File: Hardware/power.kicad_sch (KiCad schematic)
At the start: 60 parts, among them J201 Line, J202 Earth, J203 Neutral, J204 44472-0453, SW201 SW_DPST, T201 B82732R2142, T202 14A-56-28, U201 LM7912, U202 LM2574N-3.3, U203 LM2596T-5, U204 LM2596T-12

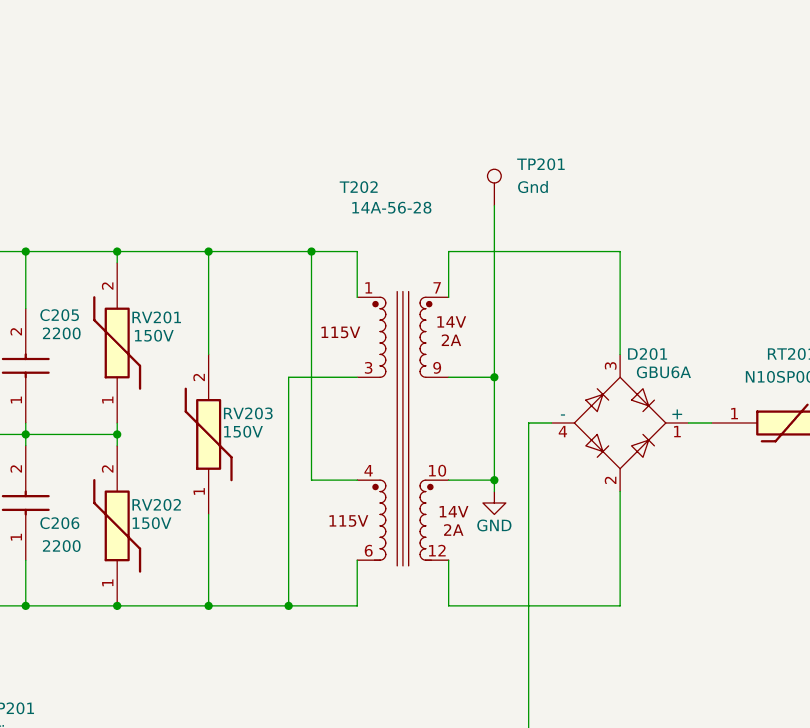
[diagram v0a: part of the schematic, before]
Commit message: updated schematics
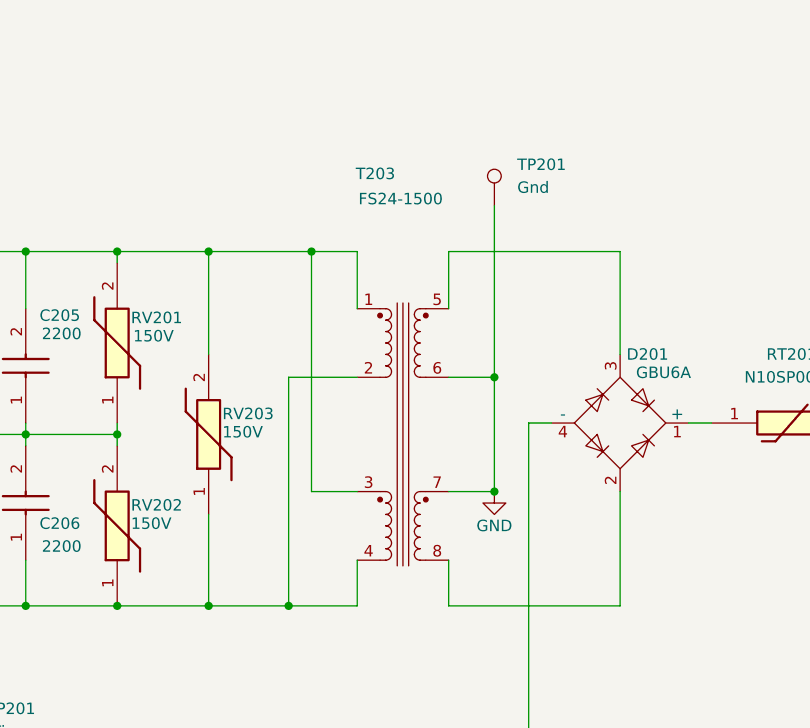
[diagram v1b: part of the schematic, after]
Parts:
- removed T202: 14A-56-28, Transformers_Signal:14A-56, symbol DH_Transformers_Power:14A-56-28
- added T203: FS24-1500, DH_Transformers_Triad:FS-36VA, symbol DH_Transformers_Triad:FS24-1500
- JP201: footprint (none) -> Jumper:SolderJumper-2_P1.3mm_Bridged_RoundedPad1.0x1.5mm
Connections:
- net GND: now also T203.6, T203.7
- net at C204.2, C205.2, RV201.2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: now also T203.1, T203.3
- net at D201.2: now also T203.8
- net at C204.1, C206.1, RV202.1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: now also T203.2, T203.4
- net at D201.3: now also T203.5
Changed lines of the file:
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@@
 	)
 	(junction
+		(at 200.66 140.97)
+		(diameter 0)
+		(color 0 0 0 0)
+	)
+	(junction
 		(at 148.59 134.62)
 		(diameter 0)
@@
 	)
 	(junction
-		(at 200.66 139.7)
-		(diameter 0)
-		(color 0 0 0 0)
-	)
-	(junction
 		(at 267.97 133.35)
 		(diameter 0)
@@
 	(wire
 		(pts
-			(xy 185.42 114.3) (xy 185.42 119.38)
+			(xy 185.42 114.3) (xy 185.42 120.65)
 		)
 		(stroke
@@
 	(wire
 		(pts
-			(xy 180.34 114.3) (xy 180.34 139.7)
+			(xy 180.34 114.3) (xy 180.34 140.97)
 		)
 		(stroke
@@
 	(wire
 		(pts
-			(xy 195.58 139.7) (xy 200.66 139.7)
+			(xy 195.58 140.97) (xy 200.66 140.97)
 		)
 		(stroke
@@
 	(wire
 		(pts
-			(xy 200.66 139.7) (xy 200.66 140.97)
-		)
-		(stroke
-			(width 0)
-			(type default)
-		)
-	)
-	(wire
-		(pts
 			(xy 307.34 90.17) (xy 339.09 90.17)
 		)
@@
 	(wire
 		(pts
-			(xy 195.58 114.3) (xy 195.58 119.38)
+			(xy 195.58 114.3) (xy 195.58 120.65)
 		)
 		(stroke
@@
 	(wire
 		(pts
-			(xy 200.66 139.7) (xy 200.66 128.27)
-		)
-		(stroke
-			(width 0)
-			(type default)
-		)
-	)
-	(wire
-		(pts
 			(xy 267.97 185.42) (xy 285.75 185.42)
 		)
@@
 	(wire
 		(pts
-			(xy 185.42 139.7) (xy 180.34 139.7)
+			(xy 185.42 140.97) (xy 180.34 140.97)
 		)
 		(stroke
@@
 	(wire
 		(pts
+			(xy 200.66 128.27) (xy 200.66 140.97)
+		)
+		(stroke
+			(width 0)
+			(type default)
+		)
+	)
+	(wire
+		(pts
 			(xy 364.49 60.96) (xy 372.11 60.96)
 		)
@@
 	)
 	(symbol
-		(lib_id "DH_Transformers_Power:14A-56-28")
-		(at 190.5 132.08 0)
-		(unit 1)
-		(exclude_from_sim no)
-		(in_bom yes)
-		(on_board yes)
-		(dnp no)
-		(property "Reference" "T202"
-			(at 185.674 107.188 0)
-			(effects
-				(font
-					(size 1.27 1.27)
-				)
-			)
-		)
-		(property "Value" "14A-56-28"
-			(at 189.23 109.474 0)
-			(effects
-				(font
-					(size 1.27 1.27)
-				)
-			)
-		)
-		(property "Footprint" "Transformers_Signal:14A-56"
-			(at 189.4991 116.84 0)
-			(effects
-				(font
-					(size 1.27 1.27)
-				)
-				(hide yes)
-			)
-		)
-		(property "Datasheet" ""
-			(at 186.69 107.188 0)
-			(effects
-				(font
-					(size 1.27 1.27)
-				)
-				(hide yes)
-			)
-		)
-		(property "Description" ""
-			(at 190.5 132.08 0)
-			(effects
-				(font
-					(size 1.27 1.27)
-				)
-				(hide yes)
-			)
-		)
-		(pin "6"
-		)
-		(pin "3"
-		)
-		(pin "4"
-		)
-		(pin "7"
-		)
-		(pin "10"
-		)
-		(pin "12"
-		)
-		(pin "9"
-		)
-		(pin "1"
-		)
-		(instances
-			(project ""
-				(path "/292023ce-4ed6-44df-ba85-3d4f8e09a45b/c5fb2ef1-a1e8-45b3-8883-b14c9804ee25"
-					(reference "T202")
-					(unit 1)
-				)
-			)
-		)
-	)
-	(symbol
 		(lib_id "Regulator_Switching:LM2574N-3.3")
 		(at 294.64 58.42 0)
@@
 			)
 		)
-		(property "Footprint" ""
+		(property "Footprint" "Jumper:SolderJumper-2_P1.3mm_Bridged_RoundedPad1.0x1.5mm"
 			(at 143.51 166.37 0)
 			(effects
@@
 					(unit 1)
 				)
+			)
+		)
+	)
+	(symbol
+		(lib_id "DH_Transformers_Triad:FS24-1500")
+		(at 187.96 133.35 0)
+		(unit 1)
+		(exclude_from_sim no)
+		(in_bom yes)
+		(on_board yes)
+		(dnp no)
+		(property "Reference" "T203"
+			(at 187.452 105.664 0)
+			(effects
+				(font
+					(size 1.27 1.27)
+				)
+			)
+		)
+		(property "Value" "FS24-1500"
+			(at 190.246 108.458 0)
+			(effects
+				(font
+					(size 1.27 1.27)
+				)
+			)
+		)
+		(property "Footprint" "DH_Transformers_Triad:FS-36VA"
+			(at 187.96 132.08 0)
+			(effects
+				(font
+					(size 1.27 1.27)
+				)
+				(hide yes)
+			)
+		)
+		(property "Datasheet" ""
+			(at 187.96 132.08 0)
+			(effects
+				(font
+					(size 1.27 1.27)
+				)
+				(hide yes)
+			)
+		)
+		(property "Description" ""
+			(at 187.96 132.08 0)
+			(effects
+				(font
+					(size 1.27 1.27)
+				)
+				(hide yes)
+			)
+		)
+		(pin "1"
+		)
+		(pin "2"
+		)
+		(pin "3"
+		)
+		(pin "4"
+		)
+		(pin "8"
+		)
+		(pin "7"
+		)
+		(pin "6"
+		)
+		(pin "5"
+		)
+		(instances
+			(project ""
+				(path "/292023ce-4ed6-44df-ba85-3d4f8e09a45b/c5fb2ef1-a1e8-45b3-8883-b14c9804ee25"
+					(reference "T203")
+					(unit 1)
+				)

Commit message: Updated PCB
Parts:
- removed C212, C215: 220, Capacitor_THT:CP_Radial_D8.0mm_P5.00mm, symbol Device:C_Polarized_US
- removed D202: 1N5819, Diode_THT:D_DO-41_SOD81_P10.16mm_Horizontal, symbol Diode:1N5819
- removed L201: 330uH, DH_Inductors:Bourns PM5022, symbol Device:L_Ferrite
- removed L204: 3.3uH, DH_Inductors:Bourns SDE04030, symbol Device:L_Ferrite
- removed R204: 1, Resistor_THT:R_Axial_DIN0204_L3.6mm_D1.6mm_P7.62mm_Horizontal, symbol Device:R_US
- removed R207: 10K, Resistor_THT:R_Axial_DIN0204_L3.6mm_D1.6mm_P7.62mm_Horizontal, symbol Device:R_US
- removed TP205: +3.3, TestPoint:TestPoint_Bridge_Pitch2.54mm_Drill1.0mm, symbol Connector:TestPoint
- removed U202: LM2574N-3.3, Package_DIP:DIP-8_W7.62mm, symbol Regulator_Switching:LM2574N-3.3
- RT201, RT202: footprint SamacSys_Parts:N10SP005M -> Capacitor_THT:C_Disc_D14.5mm_W5.0mm_P10.00mm
- TP202: value +19.8 -> +16.9
- TP203: value -19.8 -> -16.9
- renumbered C213 to C212, C214 to C213, C216 to C214, C217 to C215, D203 to D202, D204 to D203, L202 to L201, L203 to L202, L205 to L203, L206 to L204, R205 to R204, R206 to R205, R208 to R206, R209 to R207, T203 to T202, TP206 to TP205, TP207 to TP206, U203 to U202, U204 to U203

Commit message: updated pcb
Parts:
- removed SW201: SW_DPST, symbol Switch:SW_DPST
- C201, C202, C203, C204, C205, C206: footprint SamacSys_Parts:C731U222MSVDBAWL35 -> C731U222MSVDBAWL35
- J204: footprint SamacSys_Parts:44472-04YY -> 44472-04YY
- RT201: renamed from RT202; footprint Capacitor_THT:C_Disc_D14.5mm_W5.0mm_P10.00mm -> N10SP005M
- RT202: renamed from RT201; footprint Capacitor_THT:C_Disc_D14.5mm_W5.0mm_P10.00mm -> N10SP005M
- RV201, RV202, RV203: footprint SamacSys_Parts:MOV20D241KKTR -> MOV20D241KKTR
- T201: footprint SamacSys_Parts:B82732R2142B030 -> Transformers_Common_Mode_Chokes:TDK B82732R Series
- T202: footprint DH_Transformers_Triad:FS-36VA -> Transformers_Triad:FS-36VA
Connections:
- net Neutral_Filter_1: now reaches C202.1, C203.1, J204.3, T201.2
- net Line_Filter_1: now reaches C201.2, C203.2, J204.4, T201.1
- net Reg_Pos_5_Out: now reaches D202.1 (K), L201.1, U202.2 (OUT)
- net Reg_5_FB: now reaches C212.1, L201.2, L203.1, U202.4 (FB)
- net Neg_2: now reaches C208.2, C210.2, R202.2, RT201.2, TP203.1, U201.2 (VI)
- net Pos_2: now reaches C207.1, C209.1, R201.1, RT202.2, TP202.1, U202.1 (VIN), U203.1 (VIN)
- net Neg_1: now reaches D201.4 (-), RT201.1
- net Reg_Pos_12_Out: now reaches D203.1 (K), L202.1, U203.2 (OUT)
- net Reg_12_FB: now reaches C213.1, L202.2, L204.1, U203.4 (FB)
- net Line_Filter_2': now reaches C204.2, C205.2, RV201.2, RV203.2, T201.4, T202.1, T202.3
- net Line_Input: now reaches J201.1 (Pin_1), J204.2
- net Neutral_Filter_2: now reaches C204.1, C206.1, RV202.1, RV203.1, T201.3, T202.2, T202.4
- net Neutral_Input: now reaches J203.1 (Pin_1), J204.1
- net Pos_1: now reaches D201.1 (+), RT202.1
- net Secondary_1: now reaches D201.3, T202.5
- net Secondary_2: now reaches D201.2, T202.8
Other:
- moved on the sheet: C214, L201, L202, R204, RT202

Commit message: Updated Schematic; Move to SMD
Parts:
- C207, C208, C209, C210: footprint Capacitor_THT:CP_Radial_D22.0mm_P10.00mm_SnapIn -> Capacitor_SMD:CP_Elec_18x22
- C211, C212, C213: footprint Capacitor_THT:CP_Radial_D10.0mm_P5.00mm -> Capacitor_SMD:CP_Elec_10x10.5
- C214, C215: value 180 -> 150; footprint Capacitor_THT:CP_Radial_D8.0mm_P5.00mm -> Capacitor_SMD:CP_Elec_10x10
- D202, D203: footprint Diode_THT:D_DO-201AD_P15.24mm_Horizontal -> Diode_SMD:D_SOD-128
- R201, R202, R203, R204, R205, R206, R207: footprint Resistor_THT:R_Axial_DIN0204_L3.6mm_D1.6mm_P7.62mm_Horizontal -> Resistor_SMD:R_0805_2012Metric_Pad1.20x1.40mm_HandSolder
- T201: footprint Transformers_Common_Mode_Chokes:TDK B82732R Series -> DH_Transformers_Common_Mode_Chokes:TDK B82732R Series
- T202: footprint Transformers_Triad:FS-36VA -> DH_Transformers_Triad:FS-36VA
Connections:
- net Line_Filter_1: now also J204.3, T201.2; no longer J204.4, T201.1
- net Line_Filter_2': now also T201.3; no longer T201.4
- net Line_Input: now also J204.1; no longer J204.2
- net Neutral_Filter_1: now also J204.4, T201.1; no longer J204.3, T201.2
- net Neutral_Filter_2: now also T201.4; no longer T201.3
- net Neutral_Input: now also J204.2; no longer J204.1
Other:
- moved on the sheet: J204, T201
